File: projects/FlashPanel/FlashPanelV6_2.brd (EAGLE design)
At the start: 82.5 x 99.5 mm, 28 parts

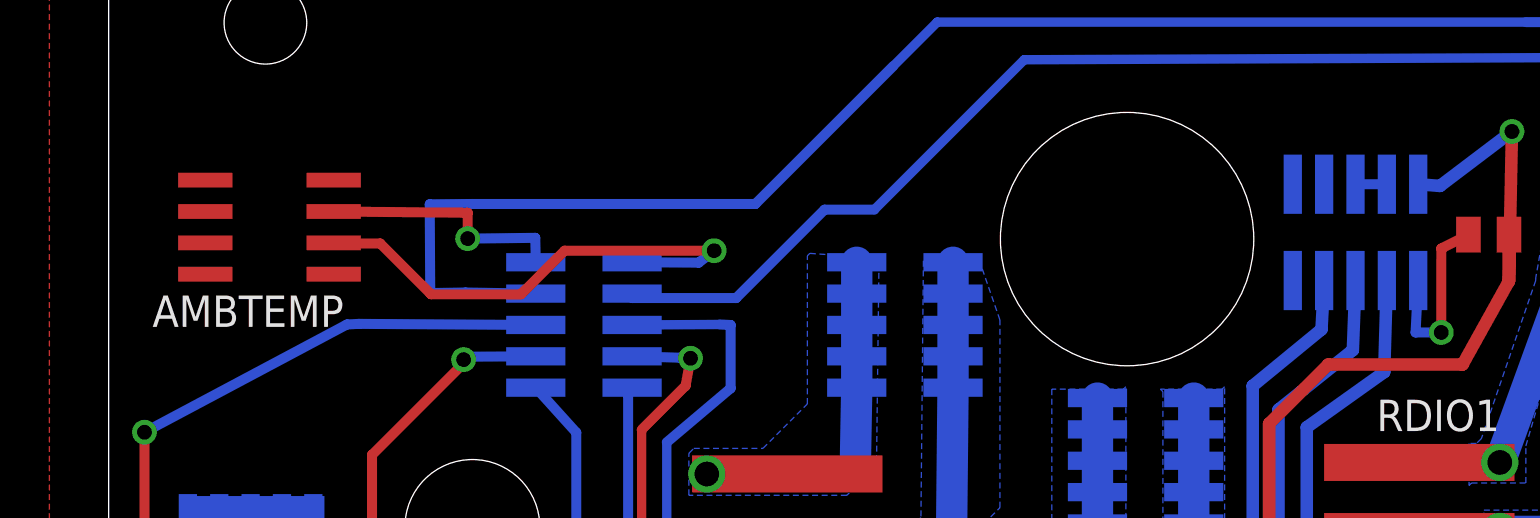
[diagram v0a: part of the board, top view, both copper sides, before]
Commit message: Small updates to Flash Panel V6.2
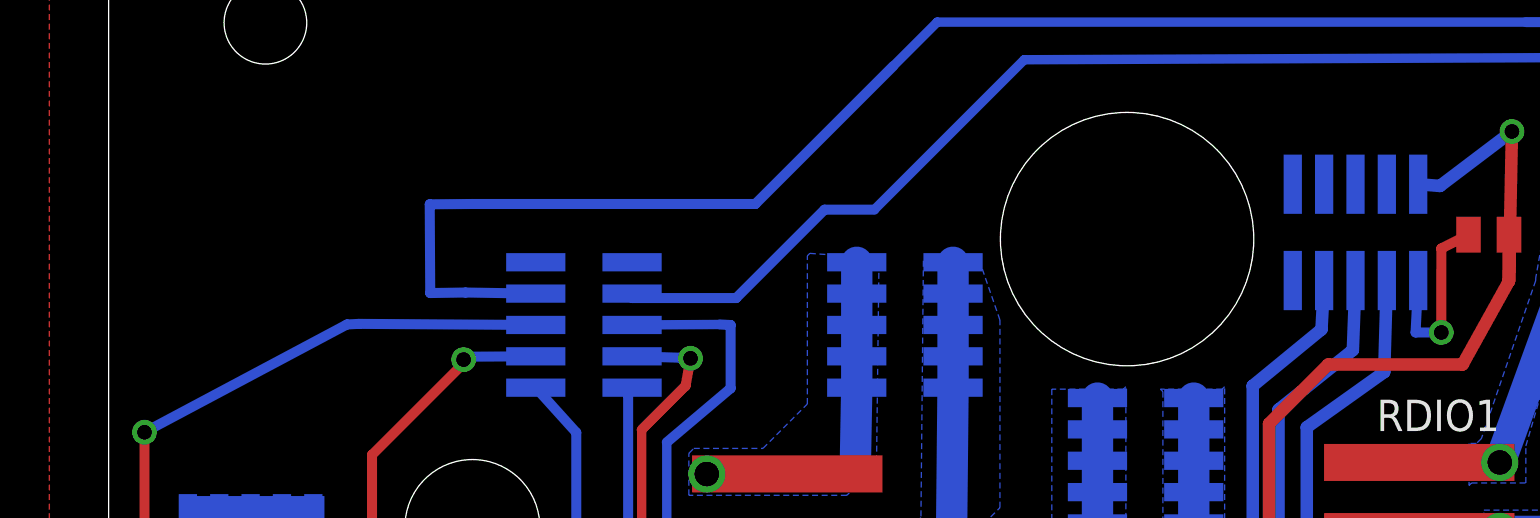
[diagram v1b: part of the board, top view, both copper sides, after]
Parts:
- removed AMBTEMP: AD590, CNTRL_BOARD:8SOIC
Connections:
- removed net N$26: AMBTEMP.3, TEMPCONNM.P5
- removed net N$27: AMBTEMP.2, TEMPCONNM.P6
- removed net TEST: CONN13M.P8, CONN13M.P9
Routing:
- net N$27: track 20.5 -> 0.00 mm, vias 1 -> 0
- net N$26: track 10.2 -> 0.00 mm, vias 1 -> 0
- net TEST: track 1.27 -> 0.00 mm
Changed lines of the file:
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@@
 <?xml version="1.0" encoding="utf-8"?>
 <!DOCTYPE eagle SYSTEM "eagle.dtd">
-<eagle version="7.6.0">
+<eagle version="7.7.0">
 <drawing>
 <settings>
@@
 <attribute name="NAME" x="23.0408" y="73.6904" size="0.75" layer="22" rot="MR0"/>
 </element>
-<element name="AMBTEMP" library="CNTRL_BOARD" package="8SOIC" value="AD590" x="6.5151" y="87.9602" smashed="yes" rot="R90">
-<attribute name="NAME" x="9.5201" y="85.1932" size="1.27" layer="25" rot="R180"/>
-<attribute name="VALUE" x="8.7032" y="91.8893" size="1" layer="27" rot="R180"/>
-</element>
 </elements>
 <signals>
@@
 <wire x1="21.204" y1="85.09" x2="21.2" y2="85.27" width="0.4064" layer="16"/>
 </signal>
-<signal name="N$26">
-<contactref element="TEMPCONNM" pad="P5"/>
-<contactref element="AMBTEMP" pad="3"/>
-<wire x1="17.3" y1="86.54" x2="17.28" y2="87.5284" width="0.4064" layer="16"/>
-<wire x1="17.28" y1="87.5284" x2="14.5415" y2="87.4976" width="0.4064" layer="16"/>
-<via x="14.5415" y="87.4976" extent="1-16" drill="0.6" shape="square"/>
-<wire x1="14.5415" y1="87.4976" x2="14.5415" y2="88.5444" width="0.4064" layer="1"/>
-<wire x1="14.5415" y1="88.5444" x2="9.1151" y2="88.5952" width="0.4064" layer="1"/>
-</signal>
-<signal name="N$27">
-<contactref element="AMBTEMP" pad="2"/>
-<contactref element="TEMPCONNM" pad="P6"/>
-<wire x1="21.2" y1="86.54" x2="23.9" y2="86.524" width="0.4064" layer="16"/>
-<wire x1="23.9" y1="86.524" x2="24.5237" y2="87.0077" width="0.4064" layer="16"/>
-<via x="24.5237" y="87.0077" extent="1-16" drill="0.6" shape="square"/>
-<wire x1="24.5237" y1="87.0077" x2="18.4658" y2="87.0077" width="0.4064" layer="1"/>
-<wire x1="18.4658" y1="87.0077" x2="16.7005" y2="85.2424" width="0.4064" layer="1"/>
-<wire x1="16.7005" y1="85.2424" x2="13.0576" y2="85.2424" width="0.4064" layer="1"/>
-<wire x1="13.0576" y1="85.2424" x2="11" y2="87.3" width="0.4064" layer="1"/>
-<wire x1="11" y1="87.3" x2="9.1403" y2="87.3" width="0.4064" layer="1"/>
-<wire x1="9.1403" y1="87.3" x2="9.1151" y2="87.3252" width="0.4064" layer="1"/>
-</signal>
-<signal name="TEST">
-<contactref element="CONN13M" pad="P9"/>
-<contactref element="CONN13M" pad="P8"/>
-<wire x1="51.77" y1="89.7" x2="50.5" y2="89.7" width="0.4064" layer="16"/>
-</signal>
 </signals>

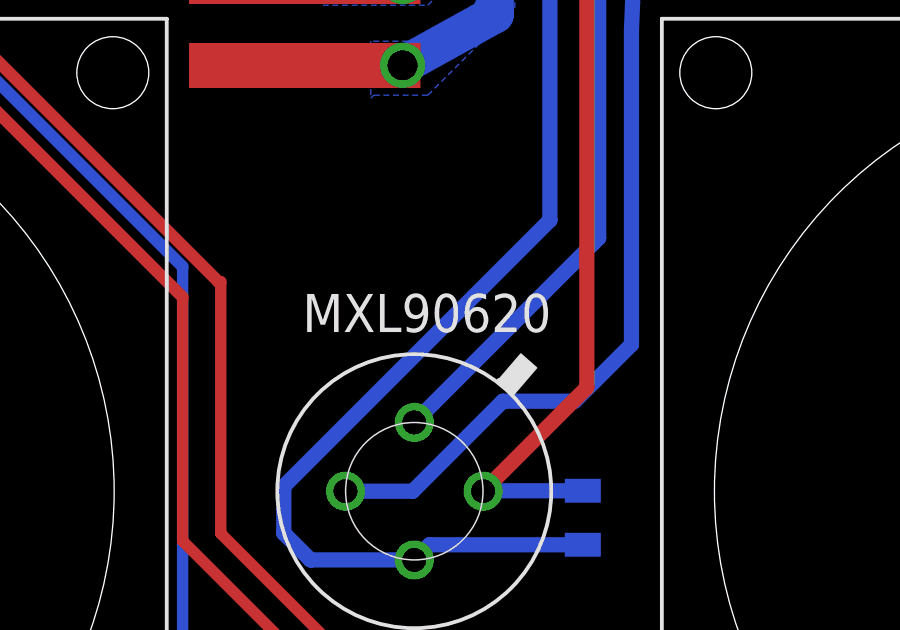
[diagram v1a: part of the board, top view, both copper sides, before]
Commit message: Cleaned up Git tracked files. Changes/additions to libraries. Addition of missing LED library part. Began Battery Board layout.
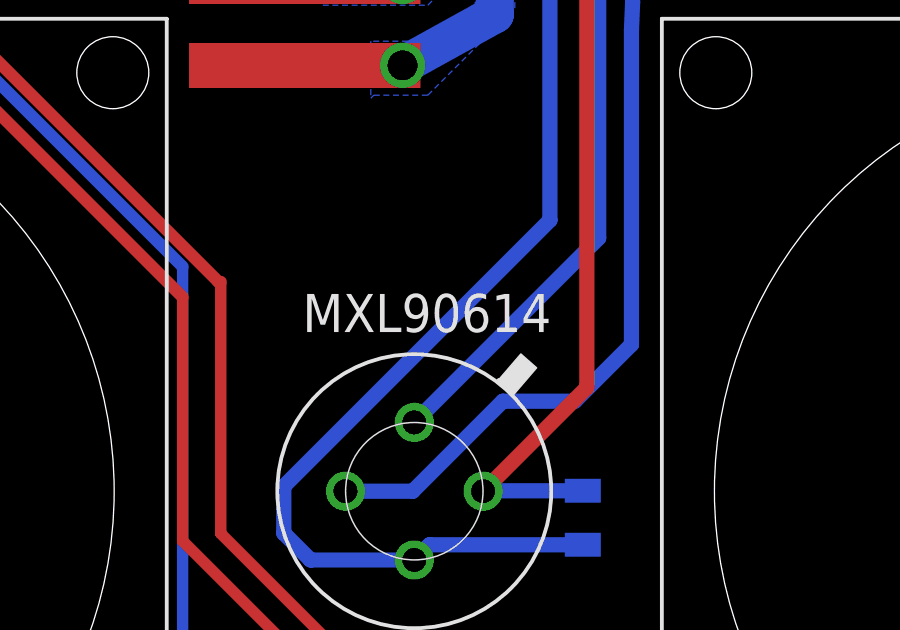
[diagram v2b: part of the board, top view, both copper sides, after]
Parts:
- U$1: value MXL90620 -> MXL90614
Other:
- board text added: "Brown Space Engineering"
- board text removed: "Brown CubeSat Team"
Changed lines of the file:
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@@
 <rectangle x1="43.70865" y1="49.90895" x2="44.17855" y2="49.92165" layer="200" rot="R180"/>
 <rectangle x1="43.77215" y1="49.92165" x2="44.11505" y2="49.93435" layer="200" rot="R180"/>
-<text x="26.3" y="98.5" size="1.778" layer="51" rot="R180">EquiSat</text>
-<text x="33.9" y="96.3" size="1.778" layer="51" rot="R180">Brown CubeSat Team</text>
+<text x="24" y="91.2" size="1.778" layer="51" rot="R180">EquiSat</text>
+<text x="32.6" y="88.4" size="1.778" layer="51" rot="R180">Brown Space Engineering</text>
 </plain>
 <attributes>
@@
 </element>
 <element name="LED4-M" library="cxm27" package="10PINMALE" value="" x="36.25" y="43.5" rot="MR90"/>
-<element name="U$1" library="CNTRL_BOARD" package="MXL90620" value="MXL90620" x="41.25" y="55" smashed="yes" rot="R90">
+<element name="U$1" library="CNTRL_BOARD" package="MXL90620" value="MXL90614" x="41.25" y="55" smashed="yes" rot="R90">
 <attribute name="VALUE" x="37.525" y="60.305" size="1.27" layer="21"/>
 </element>
